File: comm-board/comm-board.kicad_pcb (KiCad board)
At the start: 2 copper layers, 86.5 x 32.5 mm, 37 parts, among them J1 Step Down 5V, J2 Conn_01x02, J3 Conn_01x02, J4 ST-LINK, J5 Conn_01x02, J6 Power, J7 Communication, J9 Conn_01x02, U1 MAX485E, U2 LF33_TO220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

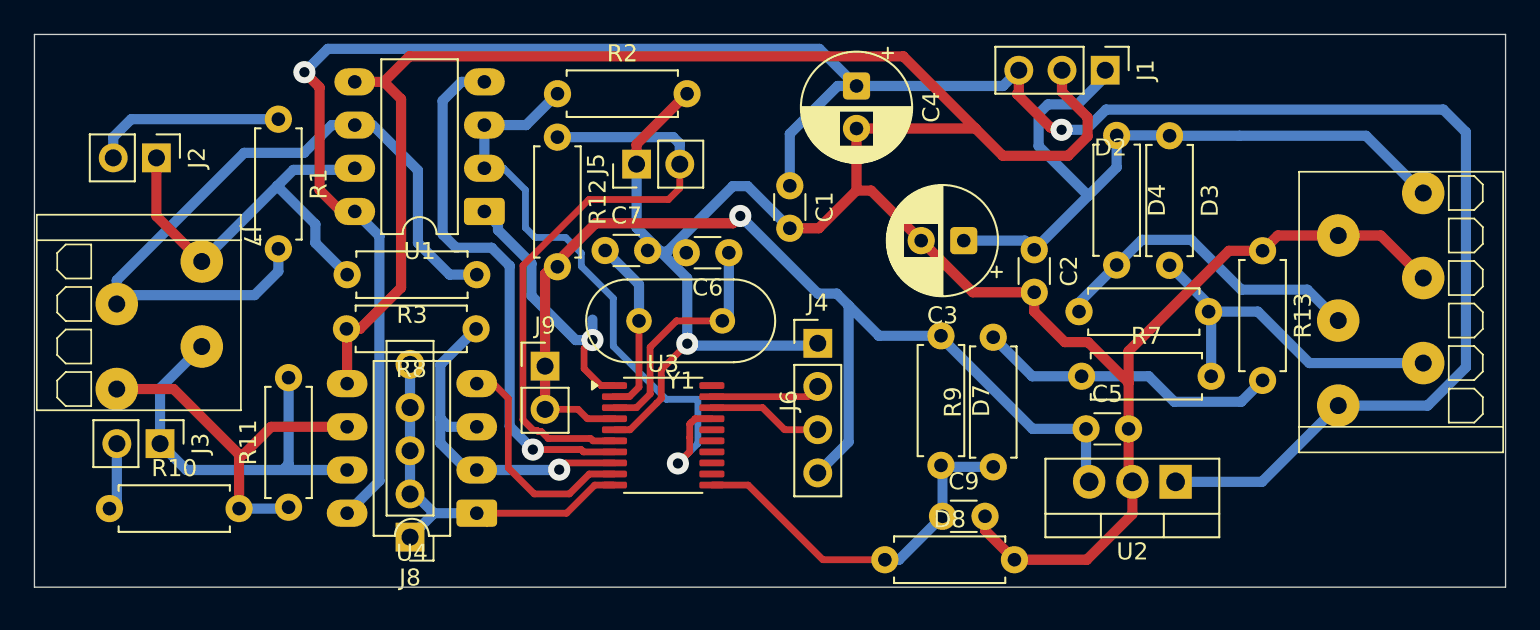
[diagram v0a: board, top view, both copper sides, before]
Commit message: PCB: comm: Cleanup and production configuration
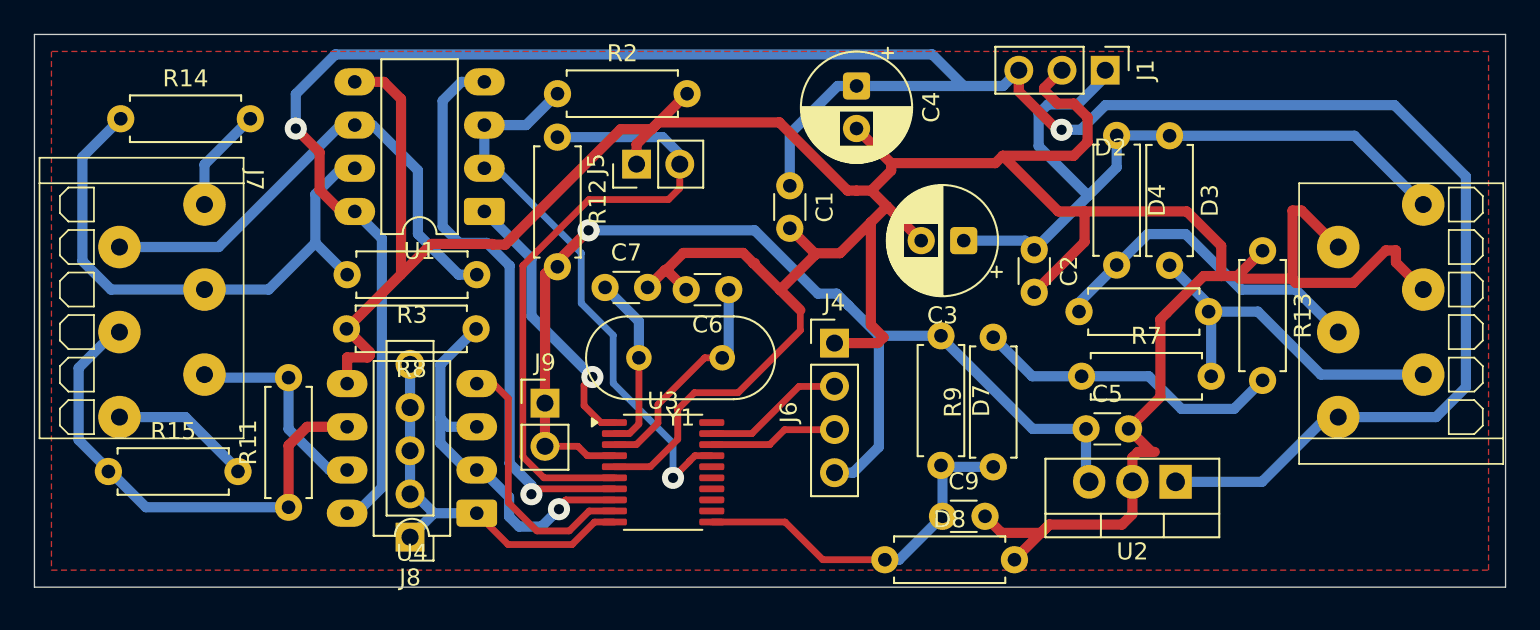
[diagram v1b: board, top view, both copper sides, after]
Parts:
- removed J2, J3: Conn_01x02, Connector_PinHeader_2.54mm:PinHeader_1x02_P2.54mm_Vertical
- removed R1, R10: 120, Resistor_THT:R_Axial_DIN0207_L6.3mm_D2.5mm_P7.62mm_Horizontal
- added R14: 120, Resistor_THT:R_Axial_DIN0207_L6.3mm_D2.5mm_P7.62mm_Horizontal, F.Cu at (105.1, 75.0)
- added R15: 120, Resistor_THT:R_Axial_DIN0207_L6.3mm_D2.5mm_P7.62mm_Horizontal, F.Cu at (104.3, 95.7)
- J7: footprint _Footprints:PTSA-0.5-4-2.5-Z -> _Footprints:PTSA-0.5-6-2.5-Z
- moved J7 3.35 mm to (110.0, 80.0)
- moved C6 2.17 mm to (140.8, 85.0)
- moved C7 2.17 mm to (133.6, 84.9)
- moved J9 2.17 mm to (130.0, 91.7)
- moved U3 2.17 mm to (137.0, 95.7)
- moved Y1 2.17 mm to (140.4, 89.0)
- moved J4 0.99 mm to (147.0, 88.1)
- moved J6 0.68 mm to (176.7, 92.5)
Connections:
- J7 pad 1: /RS-485-B1 -> Net-(J7-Pin_1)
- J7 pad 3: /RS-485-B2 -> /RS-485-B1
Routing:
- net GND: track 192.6 -> 216.1 mm, vias 1 -> 0
- net /RS-485-A1: track 44.1 -> 29.9 mm
- net Net-(J2-Pin_2): track 11.4 -> 0.00 mm
- net /RS-485-B2: track 23.9 -> 12.6 mm
- net /RS-485-B1: track 25.4 -> 33.3 mm
- net Net-(J7-Pin_6): track 0.00 -> 7.75 mm
- net /RS-485-A2: track 21.9 -> 29.3 mm
- net Net-(J7-Pin_1): track 0.00 -> 5.87 mm
- net +5V: track 144.5 -> 150.0 mm
- net Net-(J3-Pin_2): track 4.00 -> 0.00 mm
- net /DE1: track 37.5 -> 33.8 mm
- net /DE2: track 20.8 -> 23.9 mm
- net /DI1: track 31.7 -> 34.2 mm
- net /DI2: track 13.7 -> 15.7 mm
- net /SWCLK: track 6.47 -> 8.37 mm
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- added copper zone on F.Cu, net GND

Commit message: PCB: comm: Add stencil holder
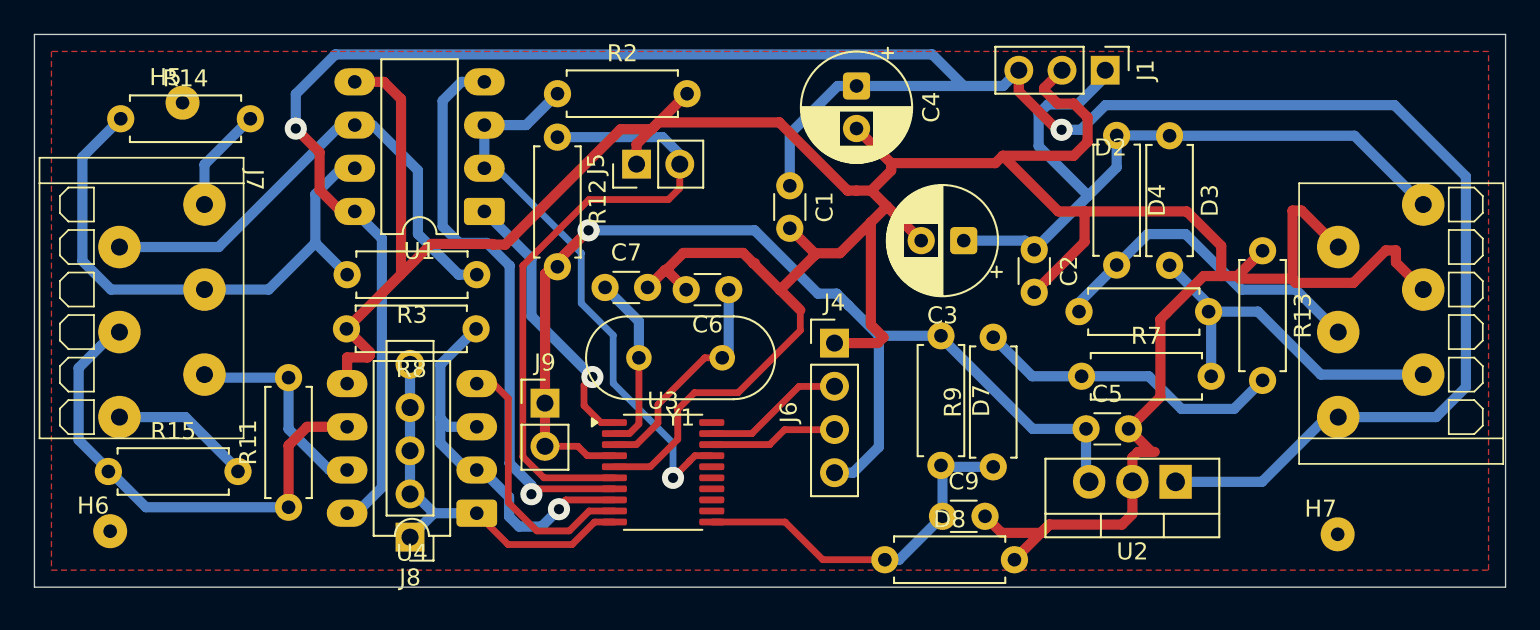
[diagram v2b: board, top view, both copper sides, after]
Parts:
- added H5: Conn_01x01, _Footprints:stencil-holder, F.Cu at (108.7, 74.0)
- added H6: Conn_01x01, _Footprints:stencil-holder, F.Cu at (104.5, 99.2)
- added H7: Conn_01x01, _Footprints:stencil-holder, F.Cu at (176.6, 99.4)
